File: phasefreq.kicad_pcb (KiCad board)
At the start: 4 copper layers, 110 x 65 mm, 111 parts, among them J1 Power Input, J2 RF Input, J3 LO Input, J4 VCO Tune, U1 LM337_SOT223, U2 LM337_SOT223, U3 LM317_3PinPackage, U4 LM337_SOT223, U5 ADCMP564, U6 AD9901, U7 LM4040DBZ-3, U8 AD8676, U9 AD8676

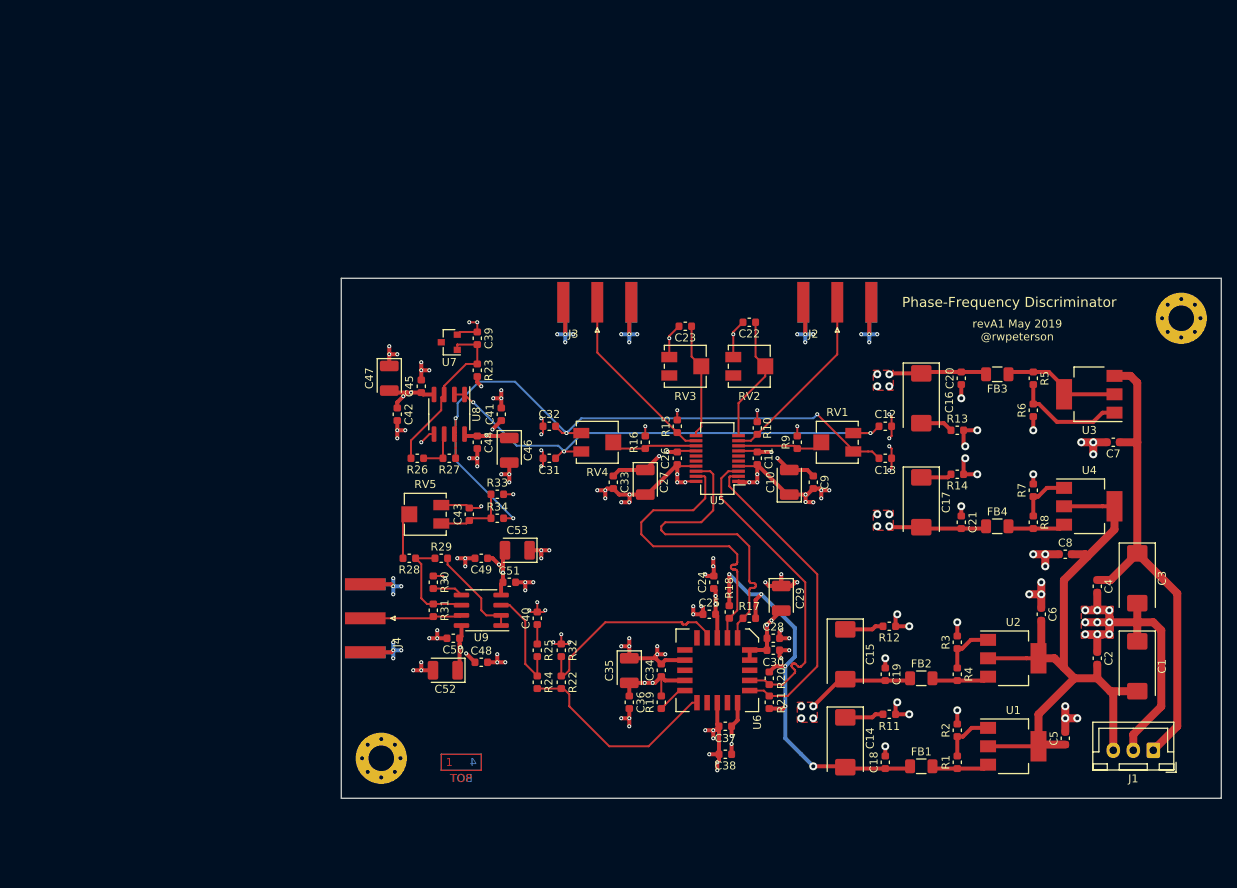
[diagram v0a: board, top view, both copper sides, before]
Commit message: fixed some cap footprints, started layout
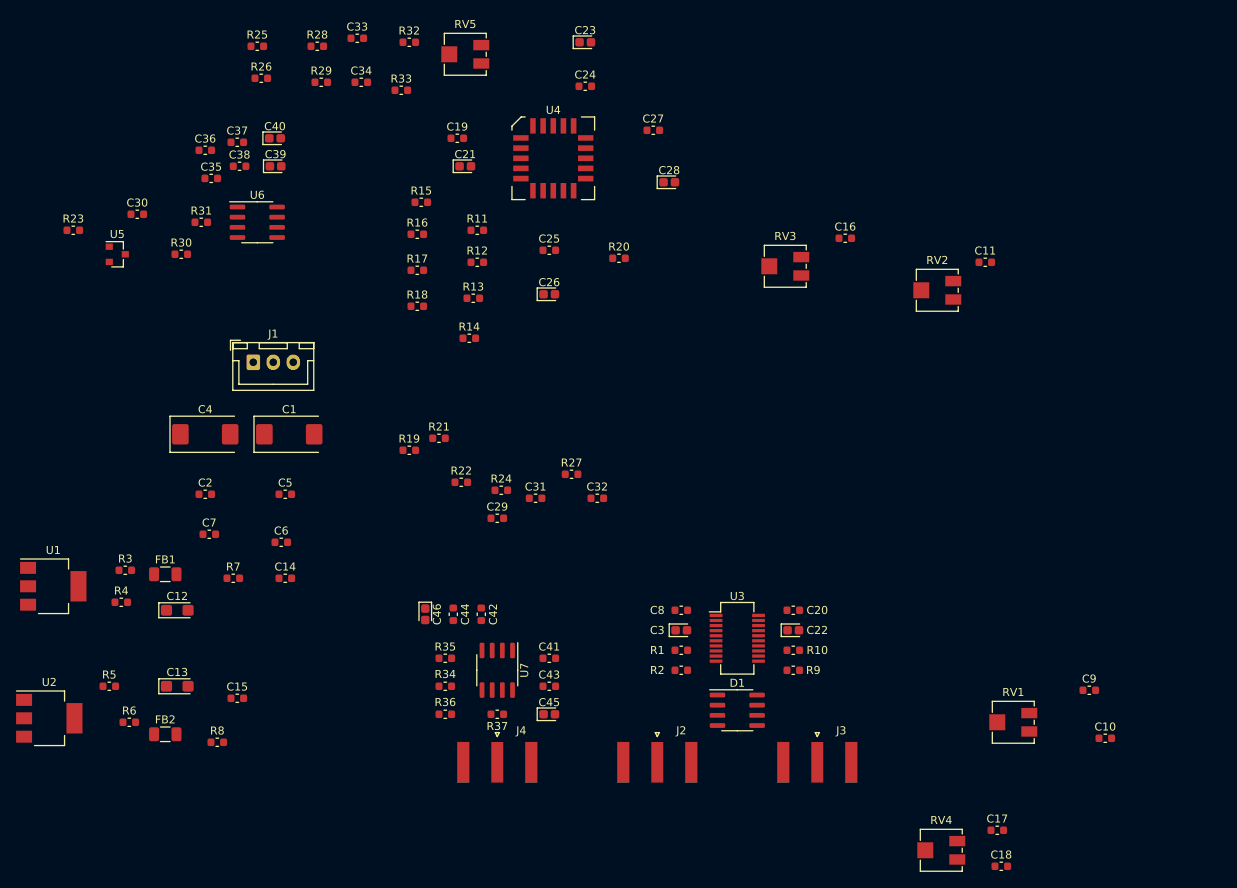
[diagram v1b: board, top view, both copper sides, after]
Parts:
- removed C47, C52, C53: 4u7, Capacitor_Tantalum_SMD:CP_EIA-3528-21_Kemet-B
- removed C48, C49: 1n, Capacitor_SMD:C_0603_1608Metric
- removed C50, C51: 100n, Capacitor_SMD:C_0603_1608Metric
- removed FB3, FB4: BLM31PG601SN1L, Inductor_SMD:L_1206_3216Metric
- removed REF** (x2): MountingHole_3.2mm_M3_Pad_Via, MountingHole:MountingHole_3.2mm_M3_Pad_Via
- removed U8, U9: AD8676, Package_SO:SOIC-8_3.9x4.9mm_P1.27mm
- added D1: SLVU2.8-8, Package_SO:SOIC-8_3.9x4.9mm_P1.27mm, F.Cu at (185.5, 126.5)
- added R35: 1K, Resistor_SMD:R_0603_1608Metric, F.Cu at (149.0, 120.0)
- added R36: 1K, Resistor_SMD:R_0603_1608Metric, F.Cu at (149.0, 127.0)
- added R37: 1K50, Resistor_SMD:R_0603_1608Metric, F.Cu at (155.5, 127.0)
- C10: value 4u7 -> 100n; footprint Capacitor_Tantalum_SMD:CP_EIA-3528-21_Kemet-B -> Capacitor_SMD:C_0603_1608Metric
- C12, C13: value 100n -> 47u; footprint Capacitor_SMD:C_0603_1608Metric -> Capacitor_Tantalum_SMD:CP_EIA-3216-18_Kemet-A
- C14, C15, C16, C17: value 47u -> 100n; footprint Capacitor_Tantalum_SMD:CP_EIA-7343-43_Kemet-X -> Capacitor_SMD:C_0603_1608Metric
- C19, C20, C25, C8: value 100n -> 10n
- C21, C22, C23, C26: value 100n -> 1u; footprint Capacitor_SMD:C_0603_1608Metric -> Capacitor_Tantalum_SMD:CP_EIA-1608-10_AVX-L
- C24: value 1n -> 10n
- C27: value 4u7 -> 10n; footprint Capacitor_Tantalum_SMD:CP_EIA-3528-21_Kemet-B -> Capacitor_SMD:C_0603_1608Metric
- C28: value 100p -> 1u; footprint Capacitor_SMD:C_0603_1608Metric -> Capacitor_Tantalum_SMD:CP_EIA-1608-10_AVX-L
- C29: value 4u7 -> 1u; footprint Capacitor_Tantalum_SMD:CP_EIA-3528-21_Kemet-B -> Capacitor_SMD:C_0603_1608Metric
- C3: value 47u -> 1u; footprint Capacitor_Tantalum_SMD:CP_EIA-7343-43_Kemet-X -> Capacitor_Tantalum_SMD:CP_EIA-1608-10_AVX-L
- C30, C34: value 10n -> 100n
- C31, C32: value 100n -> DNP
- C33: value 1n -> DNP
- C35: value 4u7 -> 1n; footprint Capacitor_Tantalum_SMD:CP_EIA-3528-21_Kemet-B -> Capacitor_SMD:C_0603_1608Metric
- C36: value 100p -> 1n
- C38, C9: value 1n -> 100n
- C39, C40, C45: value 100n -> 4u7; footprint Capacitor_SMD:C_0603_1608Metric -> Capacitor_Tantalum_SMD:CP_EIA-1608-10_AVX-L
- C4: value 100n -> 47u; footprint Capacitor_SMD:C_0603_1608Metric -> Capacitor_Tantalum_SMD:CP_EIA-7343-43_Kemet-X
- C46: footprint Capacitor_Tantalum_SMD:CP_EIA-3528-21_Kemet-B -> Capacitor_Tantalum_SMD:CP_EIA-1608-10_AVX-L
- R1: value 560 -> 49R9; footprint Capacitor_SMD:C_0603_1608Metric -> Resistor_SMD:R_0603_1608Metric
- R10, R25, R9: footprint Capacitor_SMD:C_0603_1608Metric -> Resistor_SMD:R_0603_1608Metric
- R11, R13: value 5R0 -> 80R6; footprint Capacitor_SMD:C_0603_1608Metric -> Resistor_SMD:R_0603_1608Metric
- R12, R14: value 5R0 -> 130; footprint Capacitor_SMD:C_0603_1608Metric -> Resistor_SMD:R_0603_1608Metric
- R15, R17: value 49R9 -> 80R6; footprint Capacitor_SMD:C_0603_1608Metric -> Resistor_SMD:R_0603_1608Metric
- R16, R18: value 49R9 -> 130; footprint Capacitor_SMD:C_0603_1608Metric -> Resistor_SMD:R_0603_1608Metric
- R19: value 47R5 -> 182; footprint Capacitor_SMD:C_0603_1608Metric -> Resistor_SMD:R_0603_1608Metric
- R2: value 330 -> 49R9; footprint Capacitor_SMD:C_0603_1608Metric -> Resistor_SMD:R_0603_1608Metric
- R20: value 49R9 -> 47R5; footprint Capacitor_SMD:C_0603_1608Metric -> Resistor_SMD:R_0603_1608Metric
- R21: value 49R9 -> 0R0; footprint Capacitor_SMD:C_0603_1608Metric -> Resistor_SMD:R_0603_1608Metric
- R22: value 182 -> 18K2; footprint Capacitor_SMD:C_0603_1608Metric -> Resistor_SMD:R_0603_1608Metric
- R23: value 12K1 -> 499R; footprint Capacitor_SMD:C_0603_1608Metric -> Resistor_SMD:R_0603_1608Metric
- R24: value 10K -> 110; footprint Capacitor_SMD:C_0603_1608Metric -> Resistor_SMD:R_0603_1608Metric
- R26: value 3K32 -> DNP; footprint Capacitor_SMD:C_0603_1608Metric -> Resistor_SMD:R_0603_1608Metric
- R27: value 5K00 -> 0R0; footprint Capacitor_SMD:C_0603_1608Metric -> Resistor_SMD:R_0603_1608Metric
- R28: value 1K -> DNP; footprint Capacitor_SMD:C_0603_1608Metric -> Resistor_SMD:R_0603_1608Metric
- R29: value 1K -> 0R0; footprint Capacitor_SMD:C_0603_1608Metric -> Resistor_SMD:R_0603_1608Metric
- R3: value 470 -> 330; footprint Capacitor_SMD:C_0603_1608Metric -> Resistor_SMD:R_0603_1608Metric
- R30: value 0R0 -> 1K; footprint Capacitor_SMD:C_0603_1608Metric -> Resistor_SMD:R_0603_1608Metric
- R31: value 2K74 -> 1K; footprint Capacitor_SMD:C_0603_1608Metric -> Resistor_SMD:R_0603_1608Metric
- R33: value NC -> 28K
- R34: value 0R0 -> 1K
- R4: value 150 -> 1K; footprint Capacitor_SMD:C_0603_1608Metric -> Resistor_SMD:R_0603_1608Metric
- R5: value 330 -> 1K; footprint Capacitor_SMD:C_0603_1608Metric -> Resistor_SMD:R_0603_1608Metric
- R6: value 1K -> 330; footprint Capacitor_SMD:C_0603_1608Metric -> Resistor_SMD:R_0603_1608Metric
- R7: value 1K -> 5R0; footprint Capacitor_SMD:C_0603_1608Metric -> Resistor_SMD:R_0603_1608Metric
- R8: value 330 -> 5R0; footprint Capacitor_SMD:C_0603_1608Metric -> Resistor_SMD:R_0603_1608Metric
- RV1, RV4, RV5: value 10K -> 50K
- U1: value LM337_SOT223 -> LM317_3PinPackage
- U3: value LM317_3PinPackage -> ADCMP564; footprint Package_TO_SOT_SMD:SOT-223-3_TabPin2 -> Package_SO:QSOP-20_3.9x8.7mm_P0.635mm
- U4: value LM337_SOT223 -> AD9901; footprint Package_TO_SOT_SMD:SOT-223-3_TabPin2 -> Package_LCC:PLCC-20
- U5: value ADCMP564 -> LM4040DIZ-2.5; footprint Package_SO:QSOP-20_3.9x8.7mm_P0.635mm -> Package_TO_SOT_SMD:SOT-23
- U6: value AD9901 -> AD8676; footprint Package_LCC:PLCC-20 -> Package_SO:SOIC-8_3.9x4.9mm_P1.27mm
- U7: value LM4040DBZ-3 -> AD8676; footprint Package_TO_SOT_SMD:SOT-23 -> Package_SO:SOIC-8_3.9x4.9mm_P1.27mm
- moved J1 122.5 mm to (125.0, 83.0), turned to 0 degrees
- moved R5 121.7 mm to (107.0, 123.5), turned to 0 degrees
- moved U1 121.7 mm to (100.0, 111.0)
- moved U2 120.7 mm to (99.5, 127.5)
- moved R6 119.5 mm to (109.5, 128.0), turned to 0 degrees
- moved C7 113.6 mm to (119.5, 104.5), turned to 0 degrees
- moved C2 113.4 mm to (119.0, 99.5), turned to 0 degrees
- moved C4 113.1 mm to (119.0, 92.0), turned to 0 degrees
- moved C1 109.9 mm to (129.5, 92.0), turned to 0 degrees
- moved R8 105.6 mm to (120.5, 130.5), turned to 0 degrees
- moved R4 104.9 mm to (108.5, 113.0), turned to 0 degrees
- moved R3 104.4 mm to (109.0, 109.0), turned to 0 degrees
- moved C5 102.2 mm to (129.0, 99.5), turned to 0 degrees
- moved R7 100.6 mm to (122.5, 110.0), turned to 0 degrees
- moved FB1 97.5 mm to (114.0, 109.5)
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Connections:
- C10 pad 1: GNDA -> VTUNE-
- C10 pad 2: +5VA -> GNDA
- C11 pad 1: +5VA -> Net-(C11-Pad1)
- C12 pad 1: GNDA -> VCC
- C12 pad 2: VTUNE+ -> Net-(C12-Pad2)
- C13 pad 1: VTUNE- -> Net-(C13-Pad1)
- C13 pad 2: GNDA -> VEE
- C14 pad 1: Net-(C14-Pad1) -> GNDA
- C14 pad 2: ECL_TERM -> VCC
- C15 pad 1: Net-(C15-Pad1) -> GNDA
- C15 pad 2: -5V -> VEE
- C16 pad 1: +5VA -> Net-(C16-Pad1)
- C16 pad 2: Net-(C16-Pad2) -> GNDA
- C17 pad 1: Net-(C17-Pad1) -> GNDA
- C17 pad 2: -5VA -> VTUNE+
- C18 pad 1: ECL_TERM -> VTUNE-
- C19 pad 1: GNDA -> VEE
- C19 pad 2: -5V -> GNDA
- C20 pad 1: GNDA -> VCC
- C20 pad 2: +5VA -> GNDA
- C21 pad 2: -5VA -> VEE
- C22 pad 1: Net-(C22-Pad1) -> VCC
- C23 pad 1: Net-(C23-Pad1) -> GNDA
- C23 pad 2: GNDA -> VEE
- C24 pad 1: -5V -> VEE
- C25 pad 1: GNDA -> VEE
- C25 pad 2: -5V -> GNDA
- C26 pad 1: -5VA -> GNDA
- C26 pad 2: GNDA -> VEE
- C27 pad 1: -5VA -> GNDA
- C27 pad 2: GNDA -> VEE
- C28 pad 1: -5V -> GNDA
- C28 pad 2: GNDA -> VEE
- C29 pad 1: GNDA -> Net-(C29-Pad1)
- C29 pad 2: -5V -> GNDA
- C3 pad 1: Net-(C3-Pad1) -> GNDA
- C3 pad 2: GNDA -> VEE
- C30 pad 1: -5V -> GNDA
- C30 pad 2: GNDA -> Net-(C30-Pad2)
- C31 pad 1: GNDA -> Net-(C31-Pad1)
- C31 pad 2: VTUNE+ -> GNDA
- C32 pad 1: VTUNE- -> Net-(C32-Pad1)
- C33 pad 1: -5VA -> GNDA
- C33 pad 2: GNDA -> Net-(C33-Pad2)
- C34 pad 1: -5V -> Net-(C34-Pad1)
- C35 pad 1: GNDA -> VCC
- C35 pad 2: -5V -> GNDA
- C36 pad 1: -5V -> VEE
- C37 pad 1: GNDA -> VCC
- C37 pad 2: -5V -> GNDA
- C38 pad 1: -5V -> VEE
- C39 pad 1: GNDA -> VCC
- C39 pad 2: Net-(C39-Pad2) -> GNDA
- C4 pad 1: Net-(C3-Pad1) -> Net-(C4-Pad1)
- C40 pad 1: Net-(C40-Pad1) -> GNDA
- C40 pad 2: GNDA -> VEE
- C41 pad 1: +5VA -> VCC
- C42 pad 1: -5VA -> VEE
- C43 pad 1: Net-(C43-Pad1) -> VCC
- C44 pad 1: +5VA -> VEE
- C45 pad 1: -5VA -> VCC
- C46 pad 1: +5VA -> GNDA
- C46 pad 2: GNDA -> VEE
- C5 pad 1: Net-(C1-Pad2) -> Net-(C4-Pad1)
- C6 pad 1: GNDA -> Net-(C4-Pad1)
- C6 pad 2: Net-(C1-Pad2) -> GNDA
- C7 pad 1: Net-(C3-Pad1) -> GNDA
- C7 pad 2: GNDA -> Net-(C1-Pad2)
- C8 pad 1: GNDA -> VEE
- C8 pad 2: Net-(C1-Pad2) -> GNDA
- C9 pad 1: +5VA -> GNDA
- C9 pad 2: GNDA -> VTUNE+
- FB1 pad 1: ECL_TERM -> Net-(FB1-Pad1)
- FB1 pad 2: Net-(FB1-Pad2) -> VCC
- FB2 pad 1: -5V -> VEE
- J1 pad 1: Net-(C3-Pad1) -> Net-(C4-Pad1)
- J2 pad 1: Net-(J2-Pad1) -> Net-(D1-Pad1)
- J3 pad 1: Net-(J3-Pad1) -> Net-(D1-Pad8)
- J4 pad 1: VCO_TUNE -> Net-(J4-Pad1)
- R1 pad 1: Net-(FB1-Pad2) -> Net-(D1-Pad4)
- R1 pad 2: Net-(R1-Pad2) -> GNDA
- R10 pad 1: Net-(J2-Pad1) -> Net-(D1-Pad5)
- R11 pad 1: Net-(C14-Pad1) -> GNDA
- R11 pad 2: GNDA -> ~LO_ECL~
- R12 pad 1: GNDA -> ~LO_ECL~
- R12 pad 2: Net-(C15-Pad1) -> VEE
- R13 pad 1: Net-(C16-Pad2) -> GNDA
- R13 pad 2: GNDA -> LO_ECL
- R14 pad 1: GNDA -> LO_ECL
- R14 pad 2: Net-(C17-Pad1) -> VEE
- R15 pad 1: Net-(J3-Pad1) -> GNDA
- R15 pad 2: GNDA -> RF_ECL
- R16 pad 1: Net-(R16-Pad1) -> RF_ECL
- R16 pad 2: GNDA -> VEE
- R17 pad 1: ECL_TERM -> GNDA
- R17 pad 2: ~LO_ECL~ -> ~RF_ECL~
- R18 pad 1: ECL_TERM -> ~RF_ECL~
- R18 pad 2: LO_ECL -> VEE
- R19 pad 1: Net-(R19-Pad1) -> ~PFD_OUT~
- R19 pad 2: -5V -> PFD_OUT
- R2 pad 1: Net-(R1-Pad2) -> Net-(D1-Pad1)
- R20 pad 1: ECL_TERM -> Net-(R20-Pad1)
- R20 pad 2: ~RF_ECL~ -> VEE
- R21 pad 1: RF_ECL -> GNDA
- R21 pad 2: ECL_TERM -> PFD_OUT
- R22 pad 1: PFD_OUT -> Net-(C31-Pad1)
- R23 pad 1: Net-(C39-Pad2) -> Net-(C30-Pad2)
- R23 pad 2: +5VA -> VCC
- R24 pad 1: Net-(R24-Pad1) -> Net-(C29-Pad1)
- R24 pad 2: ~PFD_OUT~ -> Net-(C31-Pad1)
- R25 pad 1: Net-(C40-Pad1) -> Net-(C33-Pad2)
- R25 pad 2: Net-(R24-Pad1) -> GNDA
- R26 pad 1: Net-(R26-Pad1) -> Net-(C34-Pad1)
- R26 pad 2: Net-(C39-Pad2) -> GNDA
- R27 pad 1: VTUNE- -> Net-(C32-Pad1)
- R27 pad 2: Net-(R26-Pad1) -> Net-(C31-Pad1)
- R28 pad 1: Net-(R28-Pad1) -> Net-(C33-Pad2)
- R28 pad 2: Net-(R28-Pad2) -> VTUNE+
- R29 pad 1: Net-(R28-Pad1) -> Net-(C34-Pad1)
- R29 pad 2: Net-(R29-Pad2) -> VTUNE-
- R3 pad 1: Net-(R3-Pad1) -> Net-(FB1-Pad1)
- R3 pad 2: GNDA -> Net-(R3-Pad2)
- R30 pad 1: GNDA -> Net-(R30-Pad1)
- R30 pad 2: Net-(R30-Pad2) -> Net-(C30-Pad2)
- R31 pad 1: Net-(R28-Pad1) -> VTUNE-
- R31 pad 2: VCO_TUNE -> Net-(R30-Pad1)
- R32 pad 1: GNDA -> Net-(R32-Pad1)
- R32 pad 2: PFD_OUT -> Net-(C33-Pad2)
- R33 pad 1: Net-(C43-Pad1) -> Net-(R33-Pad1)
- R33 pad 2: -5VA -> Net-(C34-Pad1)
- R34 pad 1: Net-(C43-Pad1) -> Net-(R34-Pad1)
- R34 pad 2: VTUNE- -> Net-(R34-Pad2)
- R4 pad 1: Net-(R3-Pad1) -> GNDA
- R4 pad 2: Net-(FB2-Pad2) -> Net-(R3-Pad2)
- R5 pad 1: Net-(FB3-Pad1) -> Net-(R5-Pad1)
- R5 pad 2: Net-(R5-Pad2) -> GNDA
- R6 pad 1: GNDA -> Net-(R5-Pad1)
- R6 pad 2: Net-(R5-Pad2) -> Net-(FB2-Pad2)
- R7 pad 1: Net-(R7-Pad1) -> Net-(C12-Pad2)
- R8 pad 1: Net-(R7-Pad1) -> GNDA
- R8 pad 2: Net-(FB4-Pad2) -> Net-(C13-Pad1)
- R9 pad 1: Net-(R9-Pad1) -> Net-(D1-Pad8)
- RV1 pad 2: Net-(R9-Pad1) -> Net-(D1-Pad4)
- RV2 pad 2: Net-(C22-Pad1) -> Net-(C11-Pad1)
- RV3 pad 2: Net-(C23-Pad1) -> Net-(C16-Pad1)
- RV4 pad 2: Net-(R16-Pad1) -> Net-(D1-Pad5)
- RV5 pad 1: GNDA -> Net-(R32-Pad1)
- RV5 pad 2: Net-(R28-Pad2) -> Net-(R34-Pad2)
- RV5 pad 3: Net-(C43-Pad1) -> Net-(R33-Pad1)
- U1 pad 1: Net-(R1-Pad2) -> Net-(R3-Pad2)
- U1 pad 2: Net-(C1-Pad2) -> Net-(FB1-Pad1)
- U1 pad 3: Net-(FB1-Pad2) -> Net-(C4-Pad1)
- U2 pad 1: Net-(R3-Pad1) -> Net-(R5-Pad1)
- U3 pad 1: Net-(R5-Pad2) -> GNDA
- U3 pad 2: Net-(FB3-Pad1) -> RF_ECL
- U3 pad 3: Net-(C3-Pad1) -> ~RF_ECL~
- U4 pad 1: Net-(R7-Pad1) -> Net-(U4-Pad1)
- U4 pad 2: Net-(C1-Pad2) -> VEE
- U4 pad 3: Net-(FB4-Pad2) -> VEE
- U5 pad 1: GNDA -> Net-(C30-Pad2)
- U5 pad 2: RF_ECL -> GNDA
- U5 pad 3: ~RF_ECL~ -> (no net)
- U6 pad 1: Net-(U6-Pad1) -> VTUNE+
- U6 pad 2: -5V -> VTUNE+
- U6 pad 3: -5V -> Net-(C30-Pad2)
- U6 pad 4: ~LO_ECL~ -> VEE
- U6 pad 5: LO_ECL -> GNDA
- U6 pad 6: -5V -> Net-(R30-Pad1)
- U6 pad 7: PFD_OUT -> VTUNE-
- U6 pad 8: Net-(U6-Pad8) -> VCC
- U7 pad 1: Net-(C39-Pad2) -> Net-(R35-Pad2)
- U7 pad 2: GNDA -> Net-(R35-Pad2)
- U7 pad 3: (no net) -> Net-(C32-Pad1)
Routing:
- net GNDA: track 330.9 -> 0.00 mm, vias 168 -> 0
- net +5VA: track 173.6 -> 0.00 mm, vias 11 -> 0
- net -5VA: track 137.3 -> 0.00 mm, vias 11 -> 0
- net -5V: track 100.3 -> 0.00 mm, vias 12 -> 0
- net VTUNE-: track 87.2 -> 0.00 mm, vias 4 -> 0
- net Net-(C1-Pad2): track 85.8 -> 0.00 mm
- net VTUNE+: track 63.0 -> 0.00 mm, vias 3 -> 0
- net Net-(C3-Pad1): track 61.1 -> 0.00 mm
- net ECL_TERM: track 54.2 -> 0.00 mm, vias 5 -> 0
- net ~LO_ECL~: track 39.7 -> 0.00 mm
- net RF_ECL: track 39.7 -> 0.00 mm
- net ~RF_ECL~: track 39.7 -> 0.00 mm
- net LO_ECL: track 39.7 -> 0.00 mm
- net ~PFD_OUT~: track 26.1 -> 0.00 mm
- net PFD_OUT: track 25.8 -> 0.00 mm
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- removed copper zone on F.Cu, net +5VA
- removed copper zone on F.Cu, net -5V
- removed copper zone on F.Cu, net -5VA
- removed copper zone on F.Cu, net GNDA
- removed copper zone on In1.Cu, net GNDA
- removed copper zone on In2.Cu, net GNDA
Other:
- board outline removed
- board text removed: "1"
- board text removed: "2"
- board text removed: "3"
- board text removed: "4"
- board text removed: "BOT"
- board text removed: "Phase-Frequency Discriminator"
- board text removed: "TOP"
- board text removed: "revA1 May 2019 @rwpeterson"

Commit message: basic layout of board, removed superfluous caps
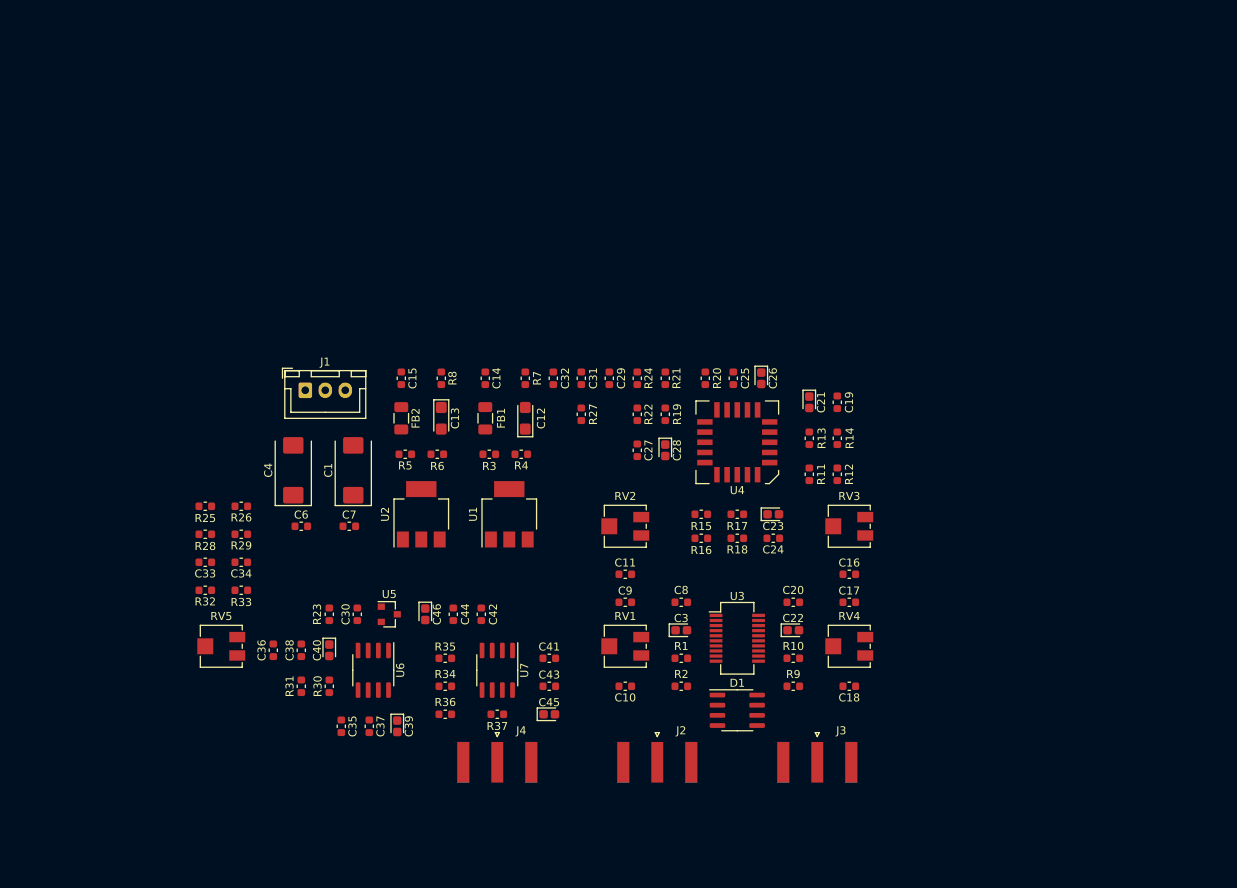
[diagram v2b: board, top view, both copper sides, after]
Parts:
- removed C2, C5: 100n, Capacitor_SMD:C_0603_1608Metric
- moved RV5 80.0 mm to (121.0, 118.5)
- moved C37 74.8 mm to (139.5, 128.5), turned to 270 degrees
- moved R32 73.1 mm to (119.0, 111.5), turned to 180 degrees
- moved C39 71.6 mm to (143.0, 128.5), turned to 270 degrees
- moved C35 70.4 mm to (136.0, 128.5), turned to 270 degrees
- moved C33 68.2 mm to (119.0, 108.0), turned to 180 degrees
- moved R33 65.6 mm to (123.5, 111.5)
- moved C40 64.4 mm to (134.5, 119.0), turned to 270 degrees
- moved C23 63.5 mm to (190.0, 102.0)
- moved C36 63.1 mm to (127.5, 119.0), turned to 90 degrees
- moved R28 62.6 mm to (119.0, 104.5)
- moved C34 61.8 mm to (123.5, 108.0), turned to 180 degrees
- moved C24 61.2 mm to (190.0, 105.0), turned to 180 degrees
- moved C38 61.0 mm to (131.0, 119.0), turned to 90 degrees
- moved C10 60.4 mm to (171.5, 123.5), turned to 180 degrees
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
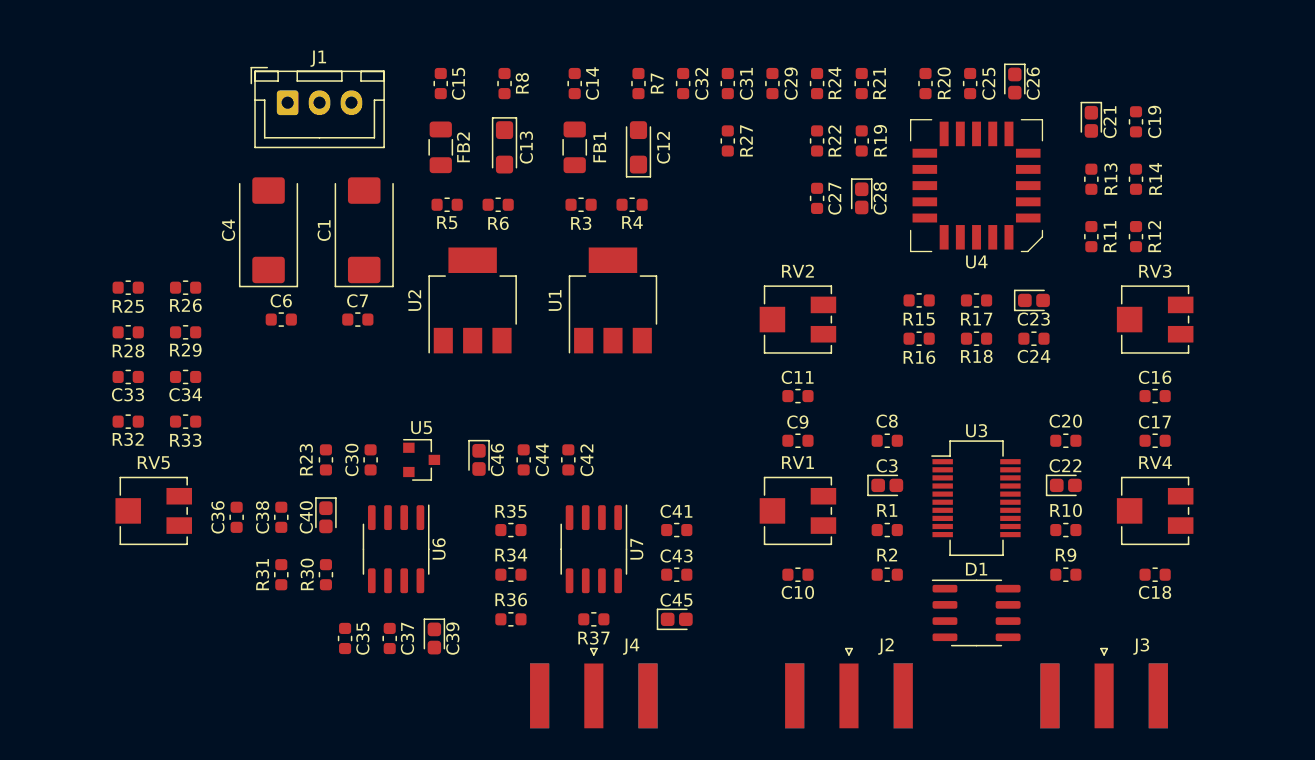
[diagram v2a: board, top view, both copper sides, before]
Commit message: routed major components, added draft board outline
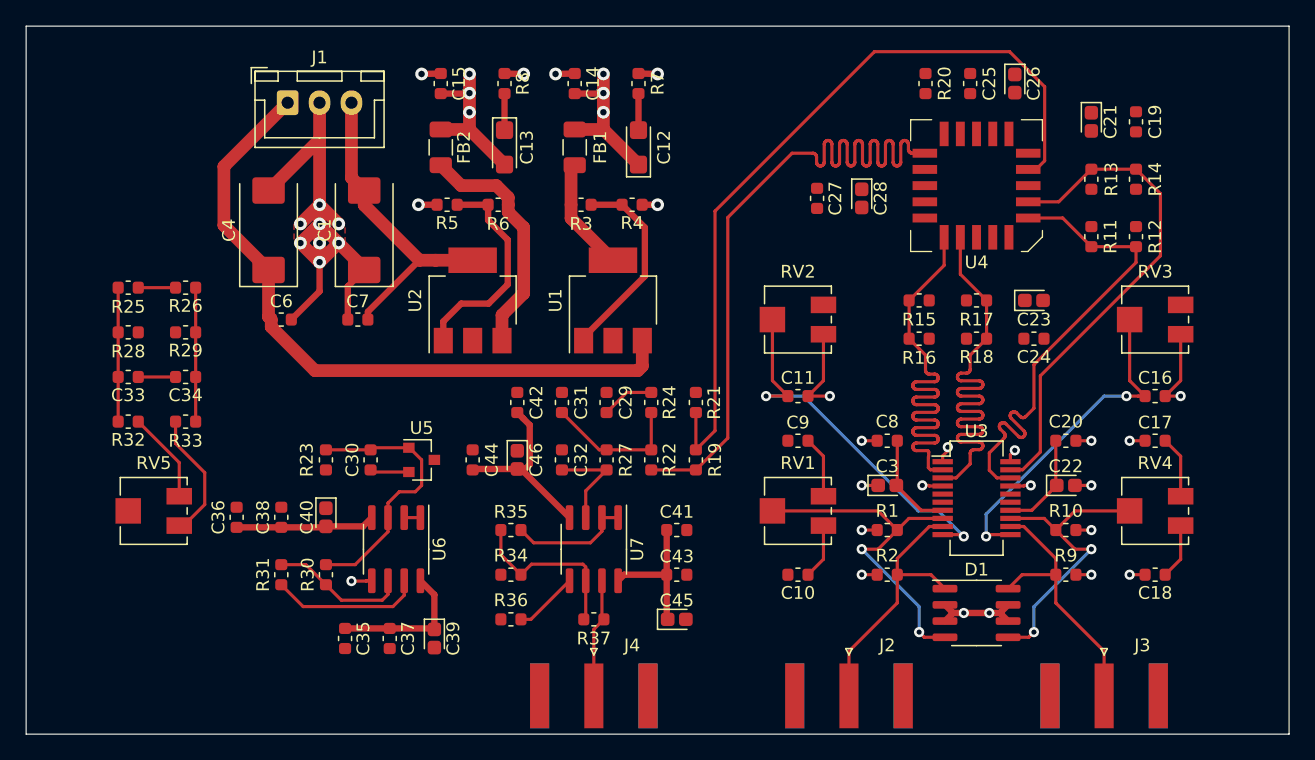
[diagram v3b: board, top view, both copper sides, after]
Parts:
- moved C32 31.0 mm to (153.0, 114.5)
- moved C29 28.2 mm to (156.5, 110.0)
- moved C31 28.2 mm to (153.0, 110.0)
- moved R19 28.2 mm to (163.5, 114.5)
- moved R21 28.2 mm to (163.5, 110.0)
- moved R22 28.2 mm to (160.0, 114.5)
- moved R24 28.2 mm to (160.0, 110.0)
- moved R27 26.7 mm to (156.5, 114.5)
- moved C42 6.02 mm to (149.5, 110.0)
- moved C44 4.00 mm to (146.0, 114.5)
- moved C46 3.00 mm to (149.5, 114.5)
- turned R12 to 90 degrees
- turned R14 to 270 degrees
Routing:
- net GNDA: track 0.00 -> 101.9 mm, vias 0 -> 33
- net ~PFD_OUT~: track 0.00 -> 62.5 mm
- net PFD_OUT: track 0.00 -> 61.8 mm
- net Net-(C4-Pad1): track 0.00 -> 53.8 mm
- net VEE: track 0.00 -> 46.4 mm, vias 0 -> 3
- net VCC: track 0.00 -> 43.1 mm, vias 0 -> 3
- net LO_ECL: track 0.00 -> 39.3 mm
- net ~RF_ECL~: track 0.00 -> 38.9 mm
- net ~LO_ECL~: track 0.00 -> 38.5 mm
- net RF_ECL: track 0.00 -> 38.4 mm
- net Net-(C11-Pad1): track 0.00 -> 30.0 mm, vias 0 -> 2
- net Net-(D1-Pad4): track 0.00 -> 28.3 mm, vias 0 -> 2
- net Net-(C16-Pad1): track 0.00 -> 26.5 mm, vias 0 -> 2
- net Net-(C1-Pad2): track 0.00 -> 25.1 mm
- net Net-(D1-Pad5): track 0.00 -> 24.3 mm, vias 0 -> 2
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- added copper zone on F.Cu, net GNDA
- added copper zone on In1.Cu, net GNDA
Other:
- board outline added: 99 x 55.5 mm
